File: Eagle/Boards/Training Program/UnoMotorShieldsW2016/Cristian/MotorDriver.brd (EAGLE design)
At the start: 64 x 66 mm, 18 parts, among them J1 ARDUINO_UNO_R3

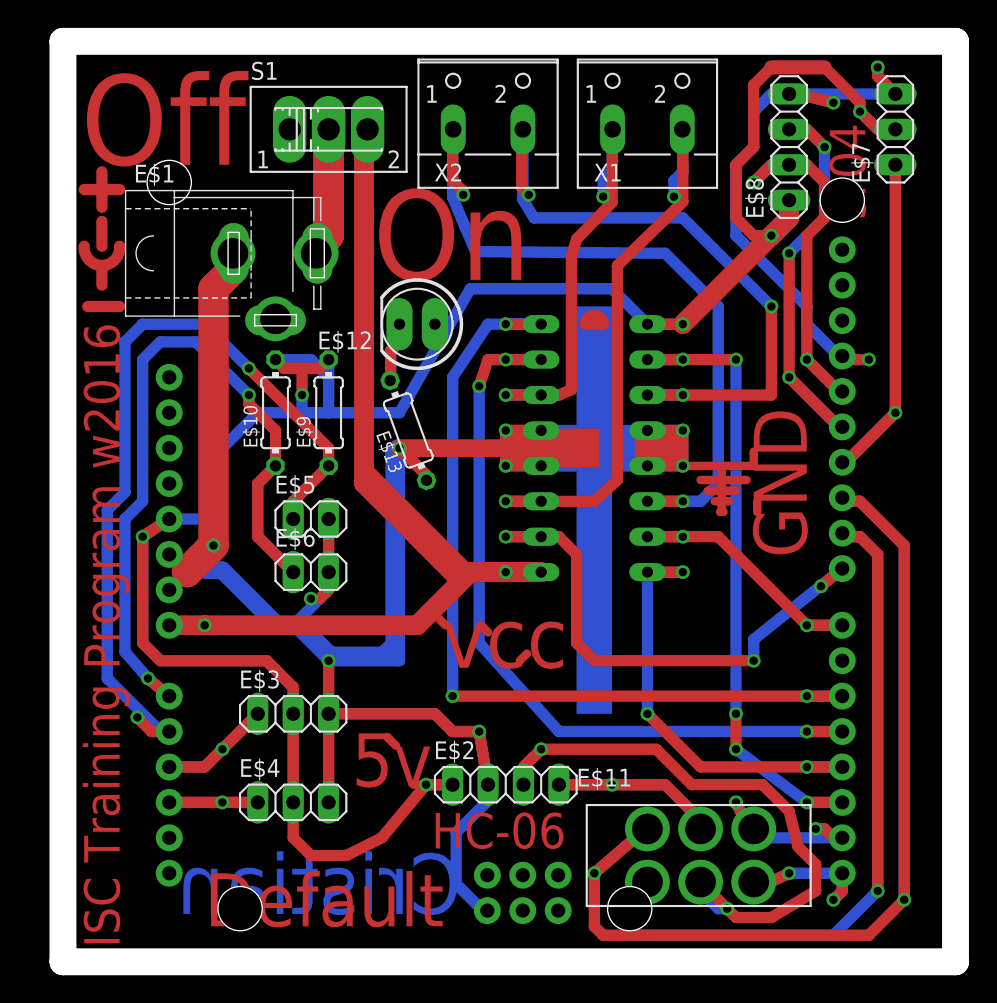
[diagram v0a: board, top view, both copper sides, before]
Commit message: updated sample motor driver shield to add directional LEDs
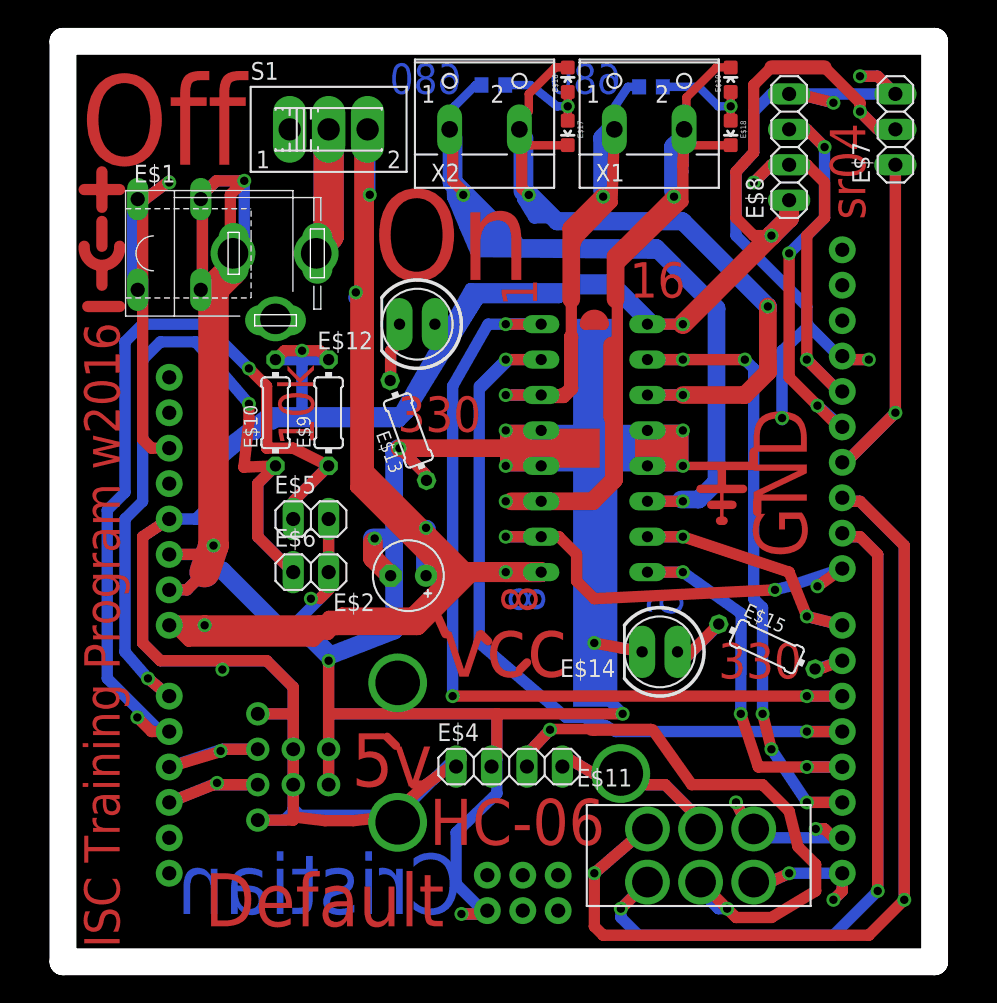
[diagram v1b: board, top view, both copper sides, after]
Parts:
- added E$14: (no value), ISCTRainingProgram:LED5MM
- added E$15: (no value), ISCTRainingProgram:0204/7
- added E$16, E$17, E$18, E$19: (no value), ISCTRainingProgram:LED-0603
- added E$20, E$21: (no value), ISCTRainingProgram:R0603
- E$2: device ISCTRainingProgram:1X04 -> ISCTRainingProgram:E2,5-5
- E$3: device ISCTRainingProgram:1X03 -> ISCTRainingProgram:BUTTON
- E$4: device ISCTRainingProgram:1X03 -> ISCTRainingProgram:1X04
- moved E$3 34.8 mm to (7.62, 51.4), flipped to the bottom, turned to 90 degrees
- moved E$2 16.5 mm to (24.8, 27.7), turned to 180 degrees
- moved E$4 15.7 mm to (32.0, 14.0)
- moved X2 0.25 mm to (30.2, 61.0)
- moved X1 0.13 mm to (42.0, 61.0)
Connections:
- removed net S$10: E$2.4
- removed net S$17: E$4.1, J1.A3
- removed net S$18: J1.A1
- new net S$42: E$14.K
- new net S$48: E$15.1
- new net S$49: E$15.2, J1.D6
- new net S$50: J1.GND@1
- new net S$66: U$1.P12, U$1.P13, U$1.P4, U$1.P5
- new net S$68: U$1.P2
- new net S$72: J1.A3
- new net S$78: J1.RESET@1
- new net S$86: E$2.+
- net N$15: no longer U$1.P2
- net N$5: no longer E$2.1, E$4.2
- net N$6: now also J1.GND@2; no longer E$2.2, E$4.3, U$1.P12, U$1.P13, U$1.P4, U$1.P5
- net S$11: now also J1.A1
- net S$16: no longer E$3.1
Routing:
- net S$66: track 0.00 -> 75.2 mm, vias 0 -> 5
- net N$5: track 187.3 -> 259.1 mm, vias 6 -> 8
- net N$7: track 137.2 -> 199.5 mm, vias 2 -> 4
- net N$6: track 202.9 -> 145.8 mm, vias 7 -> 5
- net S$11: track 16.5 -> 62.3 mm, vias 0 -> 2
- net S$18: track 44.1 -> 3.00 mm, vias 2 -> 1
- net S$46: track 4.89 -> 42.4 mm
- net S$75: track 0.00 -> 29.2 mm, vias 0 -> 1
- net S$2: track 26.9 -> 1.40 mm, vias 1 -> 0
- net N$16: track 27.1 -> 50.0 mm, vias 1 -> 2
- net S$70: track 0.00 -> 20.6 mm
- net S$78: track 0.00 -> 19.3 mm
- net S$72: track 0.00 -> 13.5 mm, vias 0 -> 2
- net S$89: track 0.00 -> 13.4 mm
- net S$26: track 39.4 -> 28.8 mm, vias 2 -> 1
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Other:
- board size 64 x 66 mm -> 62.5 x 66 mm
- board text added: "1"
- board text added: "10k"
- board text added: "16"
- board text added: "330"
- board text added: "680"
- board text added: "8"
- board text added: "9"

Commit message: updated barrel connector part
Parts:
- moved E$1 0.64 mm to (15.2, 51.4)
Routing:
- net S$75: track 29.2 -> 16.2 mm
- net S$93: track 0.00 -> 8.03 mm
- net S$94: track 0.00 -> 7.62 mm
- net S$92: track 0.00 -> 4.00 mm
- net S$91: track 0.00 -> 4.00 mm
- net S$90: track 0.00 -> 2.83 mm
- net S$12: track 63.4 -> 62.6 mm
- net S$18: vias 1 -> 0
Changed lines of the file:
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@@
 <text x="32" y="25" size="2.54" layer="16" rot="MR90">8</text>
 <text x="46.99" y="20.32" size="2.54" layer="1">330</text>
-<text x="24" y="38" size="2.54" layer="1">330</text>
+<text x="23" y="38" size="2.54" layer="1">330</text>
 <text x="18" y="37" size="2.54" layer="1" rot="R90">10k</text>
 <text x="28.575" y="62.23" size="2.1844" layer="16" rot="MR0">680</text>
@@
 <attribute name="OC_FARNELL" value="unknown" x="30.226" y="60.96" size="1.778" layer="27" display="off"/>
 </element>
-<element name="E$1" library="ISCTRainingProgram" package="5.5-2.5-BARRELCONNECTOR" value="" x="15.24" y="50.8"/>
 <element name="E$5" library="ISCTRainingProgram" package="1X02" value="" x="17.78" y="31.75"/>
 <element name="E$6" library="ISCTRainingProgram" package="1X02" value="" x="17.78" y="27.94"/>
@@
 <element name="E$4" library="ISCTRainingProgram" package="1X04" value="" x="32" y="14"/>
 <element name="E$2" library="ISCTRainingProgram" package="E2,5-5" value="" x="24.765" y="27.686" rot="R180"/>
+<element name="E$1" library="ISCTRainingProgram" package="5.5-2.5-BARRELCONNECTOR" value="" x="15.24" y="51.435"/>
 </elements>
 <signals>
@@
 <wire x1="8.89" y1="26.67" x2="10.16" y2="27.94" width="0.8128" layer="16"/>
 <wire x1="12.065" y1="50.8" x2="12.065" y2="49.53" width="2.1844" layer="1"/>
-<wire x1="12.065" y1="49.53" x2="10.795" y2="48.26" width="2.1844" layer="1"/>
-<wire x1="10.795" y1="48.26" x2="10.795" y2="29.845" width="2.1844" layer="1"/>
-<wire x1="10.795" y1="29.845" x2="10.16" y2="27.94" width="2.1844" layer="1"/>
-<wire x1="10.16" y1="27.94" x2="10.795" y2="29.845" width="2.1844" layer="16"/>
-<via x="10.795" y="29.845" extent="1-16" drill="0.6"/>
+<wire x1="12.065" y1="49.53" x2="10.295" y2="47.76" width="2.1844" layer="1"/>
+<wire x1="10.295" y1="47.76" x2="10.295" y2="29.845" width="2.1844" layer="1"/>
+<wire x1="10.295" y1="29.845" x2="10.16" y2="27.94" width="2.1844" layer="1"/>
+<wire x1="10.16" y1="27.94" x2="10.295" y2="29.845" width="2.1844" layer="16"/>
+<via x="10.295" y="29.845" extent="1-16" drill="0.6"/>
 <wire x1="7.62" y1="26.67" x2="8.89" y2="26.67" width="0.8128" layer="1"/>
 <wire x1="8.89" y1="26.67" x2="10.16" y2="27.94" width="0.8128" layer="1"/>
@@
 <wire x1="13.97" y1="30.48" x2="13.97" y2="34.29" width="0.8128" layer="1"/>
 <wire x1="13.97" y1="34.29" x2="15.24" y2="35.56" width="0.8128" layer="1"/>
-<wire x1="15.24" y1="35.56" x2="12.97" y2="35.465" width="0.8128" layer="1"/>
-<wire x1="12.97" y1="35.465" x2="13.335" y2="38.735" width="0.8128" layer="1"/>
-<via x="13.335" y="40.005" extent="1-16" drill="0.6"/>
-<wire x1="13.335" y1="38.735" x2="13.335" y2="40.005" width="0.8128" layer="1"/>
-<wire x1="13.335" y1="40.005" x2="9.525" y2="44.45" width="0.8128" layer="16"/>
+<wire x1="15.24" y1="35.56" x2="12.97" y2="35.965" width="0.8128" layer="1"/>
+<wire x1="12.97" y1="35.965" x2="12.835" y2="38.235" width="0.8128" layer="1"/>
+<via x="12.835" y="40.005" extent="1-16" drill="0.6"/>
+<wire x1="12.835" y1="38.235" x2="12.835" y2="40.005" width="0.8128" layer="1"/>
+<wire x1="12.835" y1="40.005" x2="9.525" y2="44.45" width="0.8128" layer="16"/>
 <wire x1="9.525" y1="44.45" x2="6.985" y2="44.45" width="0.8128" layer="16"/>
 <wire x1="6.985" y1="44.45" x2="5.715" y2="43.18" width="0.8128" layer="16"/>
@@
 </signal>
 <signal name="S$18">
-<via x="22" y="55" extent="1-16" drill="0.6"/>
 <wire x1="22" y1="55" x2="22" y2="58" width="0.8128" layer="16"/>
 </signal>
@@
 </signal>
 <signal name="S$75">
-<wire x1="10" y1="48" x2="10" y2="55" width="0.8128" layer="16"/>
 <wire x1="10" y1="55" x2="11" y2="56" width="0.8128" layer="16"/>
 <via x="13" y="56" extent="1-16" drill="0.6"/>
@@
 <wire x1="13" y1="56" x2="11" y2="56" width="0.8128" layer="1"/>
 <wire x1="11" y1="56" x2="10" y2="55" width="0.8128" layer="1"/>
-<wire x1="10" y1="55" x2="10" y2="49" width="0.8128" layer="1"/>
 <wire x1="11" y1="56" x2="13" y2="56" width="0.8128" layer="16"/>
 <wire x1="13" y1="56" x2="13" y2="51" width="0.8128" layer="16"/>
@@
 <wire x1="24" y1="10.5" x2="28" y2="14.5" width="0.8128" layer="16"/>
 </signal>
+<signal name="S$90">
+<wire x1="10" y1="48" x2="12" y2="50" width="1.016" layer="16"/>
+</signal>
+<signal name="S$91">
+<wire x1="23" y1="43.5" x2="23" y2="47.5" width="0.6096" layer="1"/>
+</signal>
+<signal name="S$92">
+<wire x1="40.5" y1="20.5" x2="40.5" y2="24.5" width="0.6096" layer="1"/>
+</signal>
+<signal name="S$93">
+<wire x1="44" y1="24.5" x2="44.5" y2="20.5" width="0.6096" layer="1" curve="-180"/>
+<wire x1="27" y1="47.5" x2="27" y2="43.5" width="0.6096" layer="1" curve="-180"/>
+</signal>
+<signal name="S$94">
+<wire x1="28.5" y1="44" x2="28.5" y2="43" width="0.6096" layer="1"/>
+<wire x1="28.5" y1="43" x2="30" y2="41.5" width="0.6096" layer="1"/>
+<wire x1="30" y1="41.5" x2="30" y2="37" width="0.6096" layer="1"/>
+</signal>
 </signals>
